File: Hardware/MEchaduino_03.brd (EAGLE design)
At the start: 41.9 x 41.9 mm, 45 parts, among them Q2 NFET, U1 TLV70233PDBVR, U2 ATSAMD51G-M, U3 TXB0104, Y2 32,768Khz

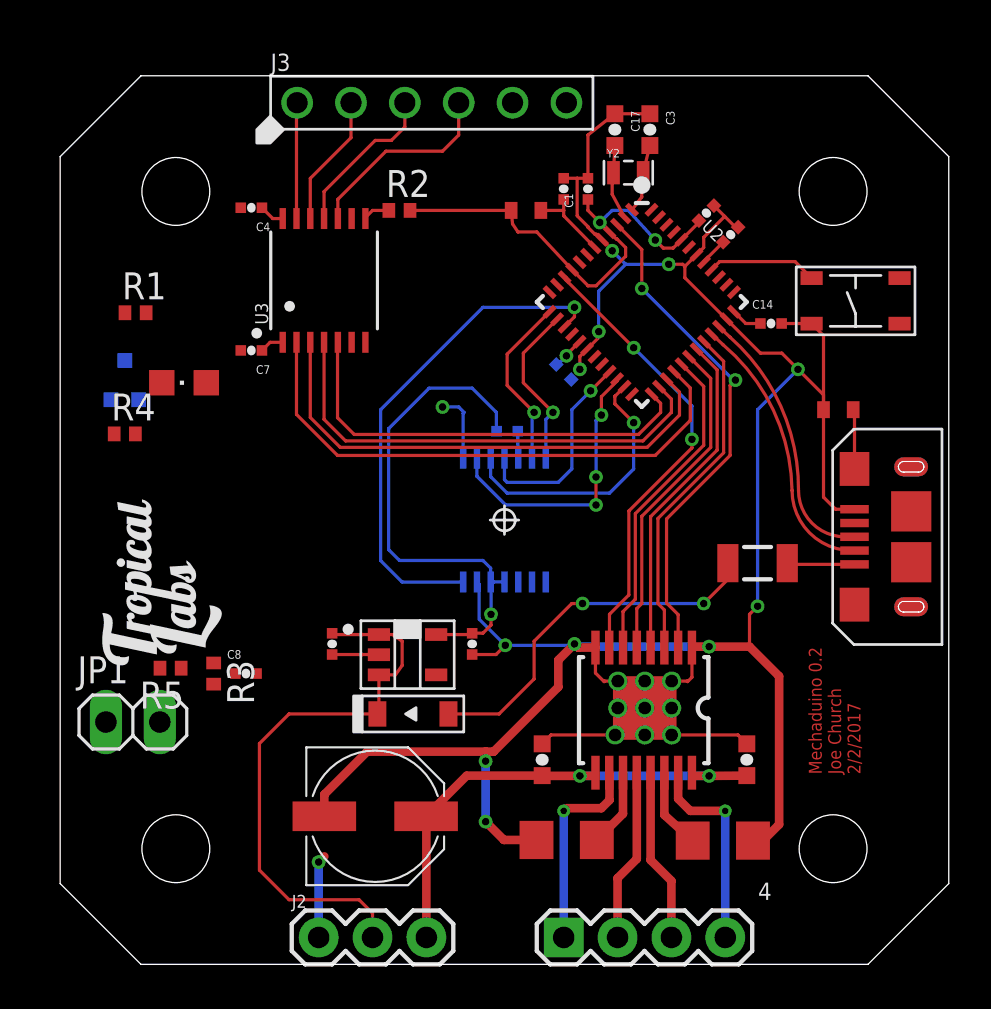
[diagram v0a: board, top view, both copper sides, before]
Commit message: changed microcontroller to ATSAMD51J19
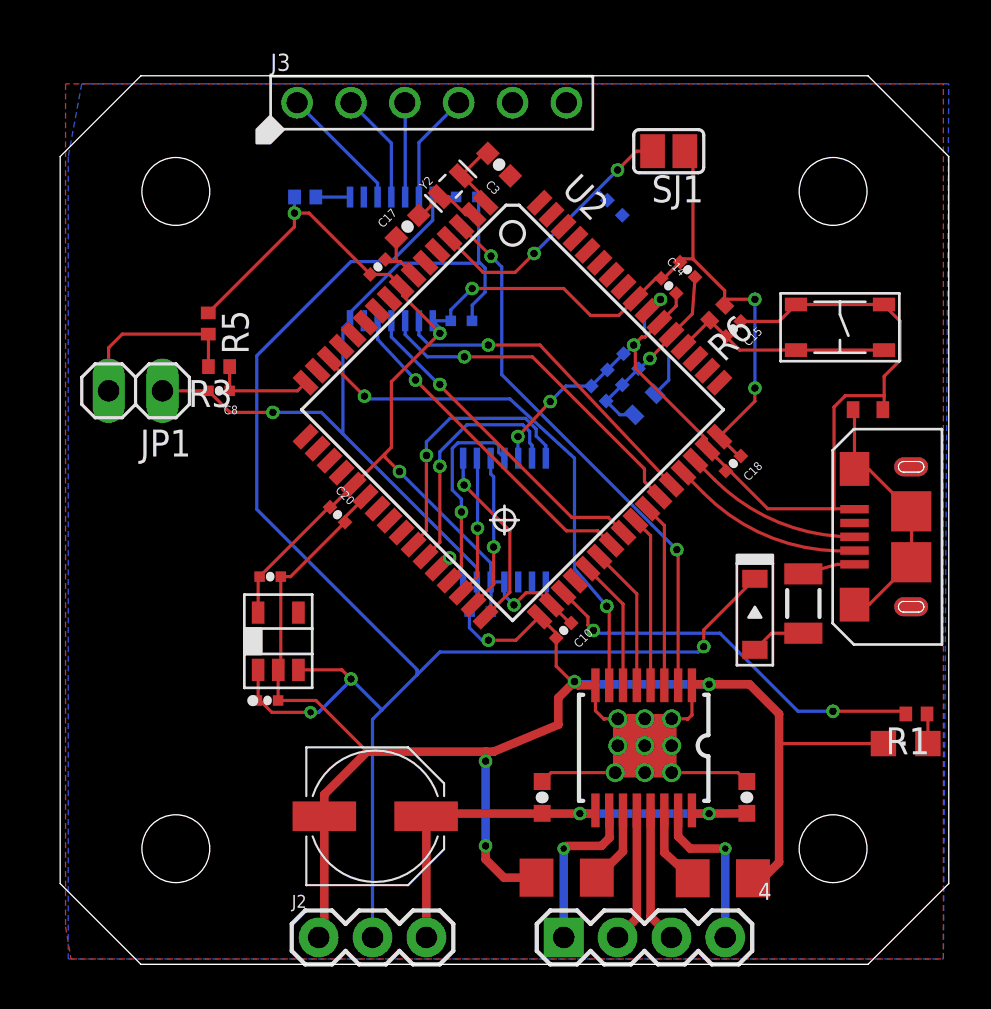
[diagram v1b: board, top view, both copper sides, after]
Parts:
- removed Q2: NFET, SparkFun-DiscreteSemi:SOT323
- removed R4: 100k, rcl:R0402
- removed U$3: TROPICAL_LABS_LOGO_1LOGO3, stepper_servo_prototype_1:LOGO3
- added C15, C18, C20, C21, C22: 0.1uF, swift:0402-CAP
- added R6: 10k, rcl:R0402
- added SJ1: (no value), jumper:SJ
- C17, C3: value 18pF -> 22pF
- R1: value 330 -> 1k
- U2: value ATSAMD51G-M -> ATSAMD51J19; device atsamd51:QFN-48 -> atsamd51:TQFP64
- moved R1 41.4 mm to (40.4, 11.8), turned to 180 degrees
- moved LED1 38.1 mm to (39.9, 10.4)
- moved D1 16.8 mm to (32.8, 16.5), turned to 270 degrees
- moved R5 16.4 mm to (6.99, 30.2), turned to 270 degrees
- moved C2 15.7 mm to (15.0, 32.9)
- moved JP1 15.6 mm to (3.56, 27.1), turned to 180 degrees
- moved R3 14.5 mm to (7.49, 28.2), turned to 180 degrees
- moved C8 13.4 mm to (7.49, 27.1), turned to 180 degrees
- moved C10 12.2 mm to (23.7, 15.7), flipped to the top
- moved C17 10.8 mm to (16.4, 34.8), turned to 45 degrees
- moved L2 10.7 mm to (27.6, 26.4), flipped to the bottom, turned to 135 degrees
- moved C4 10.2 mm to (19.2, 36.2), flipped to the bottom
- moved C19 10.0 mm to (9.91, 18.3), turned to 0 degrees
- moved C7 10.0 mm to (18.9, 30.4), flipped to the bottom
- moved C1 8.98 mm to (26.2, 27.7), flipped to the bottom, turned to 45 degrees
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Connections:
- net PA00_XIN1 renamed CRYST1
- net PA01_XOUT1 renamed CRYST2
- removed net ARDUINO_D13_SCK: Q2.1, R4.2
- removed net GND2: J2.1
- removed net HEADER_MISO: U$4.3, U2.23
- removed net HEADER_MOSI: U$4.4, U2.21
- removed net HEADER_SCK: U$4.2, U2.22
- removed net HEADER_SS: U$4.1, U2.11
- removed net N$11: J3.P$4, U3.10
- removed net N$12: J3.P$3, U3.11
- removed net N$17: J3.P$2, U3.12
- removed net N$18: J3.P$1, U3.13
- removed net N$3: Q2.3, R1.1
- removed net SCL: U2.48
- removed net SDA: U2.47
- removed net TARGET_USB_N: J1.2, U2.33
- removed net TARGET_USB_P: J1.3, U2.34
- removed net VDDANA: C5.1, L2.2, U2.6
- new net AREF: C22.1, SJ1.2, U2.4
- new net D+: J1.3, U2.46
- new net D-: J1.2, U2.45
- new net D13: R1.2, U2.35
- new net MISO: U$4.3, U2.31
- new net MOSI: U$4.4, U2.29
- new net N$10: L2.2, U2.55
- new net N$2: J3.P$4, U3.13
- new net N$4: J3.P$3, U3.12
- new net SCK: U$4.2, U2.30
- new net SS: U$4.1, U2.32
- net 3.3V: now also C10.1, C11.2, C14.1, C18.1, C20.1, R6.1, SJ1.1, U2.21, U2.34, U2.48, U2.56, U2.8; no longer C1.1, L2.1, LED1.A, U2.4, U2.44, U2.9
- net A: now also U2.27; no longer U2.13
- net ARDUINO_D0: now also U2.44, U3.2; no longer U2.25, U3.5
- net ARDUINO_D1: now also U2.43, U3.3; no longer U2.26, U3.4
- net ARDUINO_D2: now also U2.40, U3.4; no longer U2.27, U3.3
- net ARDUINO_D3: now also U2.39, U3.5; no longer U2.28, U3.2
- net B: now also U2.26; no longer U2.14
- net GND: now also C15.1, C18.2, C20.2, C21.2, C22.2, J2.1, LED1.C, SW2.P$4, U2.22, U2.33, U2.47, U2.54, U2.7; no longer C11.2, Q2.2, R4.1, U2.18, U2.35, U2.42, U2.5
- net I: now also U2.28; no longer U2.15
- net IN1: now also U2.37; no longer U2.29
- net IN2: now also U2.38; no longer U2.30
- net IN3: now also U2.42; no longer U2.32
- net IN4: now also U2.41; no longer U2.31
- net N$1: now also LED1.A, R1.1; no longer LED1.C, R1.2
- net N$5: now also J3.P$2, U3.11; no longer C14.1, U2.36
- net N$7: now also J3.P$1, U3.10; no longer C10.1, U2.17
- net N$8: now also C1.1, C21.1, C5.1, L2.1, U2.53; no longer U2.41
- net RESET: now also C15.2, R6.2, SW2.P$2, U2.52; no longer U2.40
- net TH1: now also U2.16; no longer U2.8
- net VREF1: now also U2.14; no longer U2.10
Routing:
- net GND: track 127.9 -> 195.7 mm, vias 19 -> 17
- net VIN: track 28.7 -> 74.6 mm, vias 0 -> 3
- net 3.3V: track 47.7 -> 82.0 mm, vias 3 -> 7
- net I: track 23.7 -> 2.18 mm
- net D13: track 0.00 -> 18.7 mm, vias 0 -> 2
- net N$33: track 17.6 -> 2.61 mm, vias 2 -> 0
- net HEADER_SCK: track 13.4 -> 0.00 mm, vias 3 -> 0
- net AREF: track 0.00 -> 13.3 mm, vias 0 -> 2
- net HEADER_MISO: track 12.9 -> 0.00 mm, vias 1 -> 0
- net TARGET_USB_N: track 12.5 -> 0.00 mm
- net TARGET_USB_P: track 12.2 -> 0.00 mm
- net ARDUINO_D3: track 26.1 -> 16.0 mm, vias 0 -> 1
- net HEADER_MOSI: track 9.83 -> 0.00 mm, vias 1 -> 0
- net MOSI: track 0.00 -> 9.70 mm, vias 0 -> 1
- net N$11: track 9.39 -> 0.00 mm
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- added copper zone on layer 1, net GND
- added copper zone on layer 16, net GND
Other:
- board text removed: "Mechaduino 0.2 Joe Church 2/2/2017"

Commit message: implemted voltage sense pin and some leds
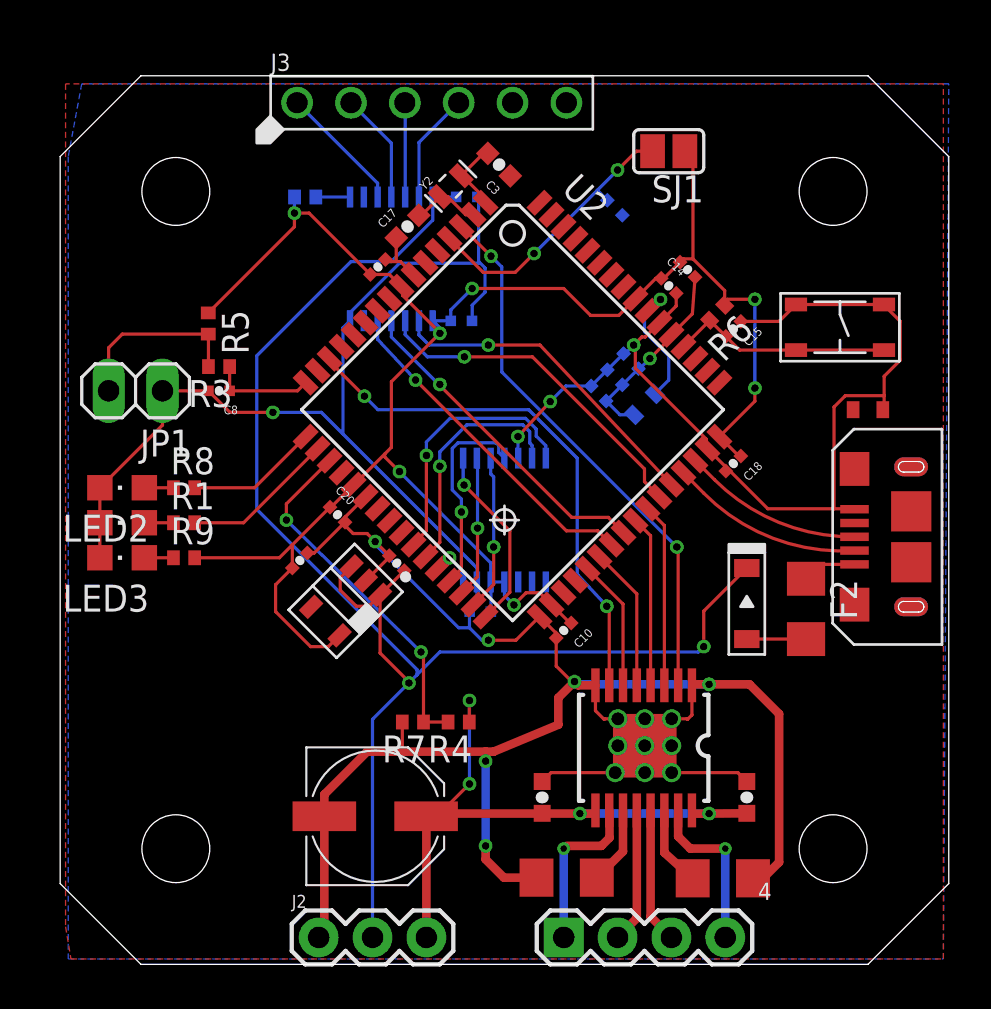
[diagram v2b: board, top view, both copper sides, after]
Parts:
- removed F1: 500mA, SparkFun-PowerIC:PTC-1206
- added F2: 500mA, adafruit:R1206
- added LED2: Red, Opto:CHIPLED_0805
- added LED3: Green, Opto:CHIPLED_0805
- added R4: 100k, rcl:R0402
- added R7: 6k8, rcl:R0402
- added R8, R9: 1k, rcl:R0402
- J1: value (none) -> USB
- J2: value (none) -> power
- J3: value (none) -> signals
- JP1: value (none) -> thermistor
- JP6: value (none) -> Motor
- SJ1: value (none) -> vref
- SW2: value (none) -> Reset
- moved LED1 38.4 mm to (2.92, 20.8)
- moved R1 35.7 mm to (5.84, 20.8), turned to 0 degrees
- moved C9 8.89 mm to (15.9, 18.9), turned to 135 degrees
- moved U1 3.70 mm to (13.5, 17.1), turned to 225 degrees
- moved C19 1.59 mm to (11.3, 19.1), turned to 45 degrees
- moved D1 0.63 mm to (32.4, 17.0)
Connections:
- net SHIELD renamed N$9
- net VIN renamed +5V
- removed net D13: R1.2, U2.35
- removed net N$33: D1.ANODE, F1.2
- new net LEDERROR: R8.2, U2.17
- new net LEDSTATUS: R1.2, U2.18
- new net N$11: LED3.A, R9.1
- new net N$12: D1.ANODE, F2.2
- new net N$3: LED2.A, R8.1
- new net VSENSE: R4.2, R7.1, U2.19
- net 3.3V: now also R9.2
- net GND: now also LED2.C, LED3.C, R7.2
- net N$36: now also F2.1; no longer F1.1
- net V+: now also R4.1
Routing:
- net D13: track 18.7 -> 0.00 mm, vias 2 -> 0
- net VSENSE: track 0.00 -> 17.0 mm, vias 0 -> 2
- net N$9: track 12.3 -> 0.00 mm
- net 3.3V: track 82.0 -> 90.4 mm
- net V+: track 22.7 -> 30.3 mm, vias 2 -> 4
- net LEDSTATUS: track 0.00 -> 7.25 mm
- net LEDERROR: track 0.00 -> 6.23 mm
- net GND: track 195.7 -> 199.2 mm, vias 17 -> 18
- net N$12: track 0.00 -> 2.79 mm
- net N$33: track 2.61 -> 0.00 mm
- net N$3: track 0.00 -> 1.37 mm
- net N$11: track 0.00 -> 1.37 mm
- net +5V: track 74.6 -> 73.5 mm, vias 3 -> 2

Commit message: Rearange to fit old pin positions
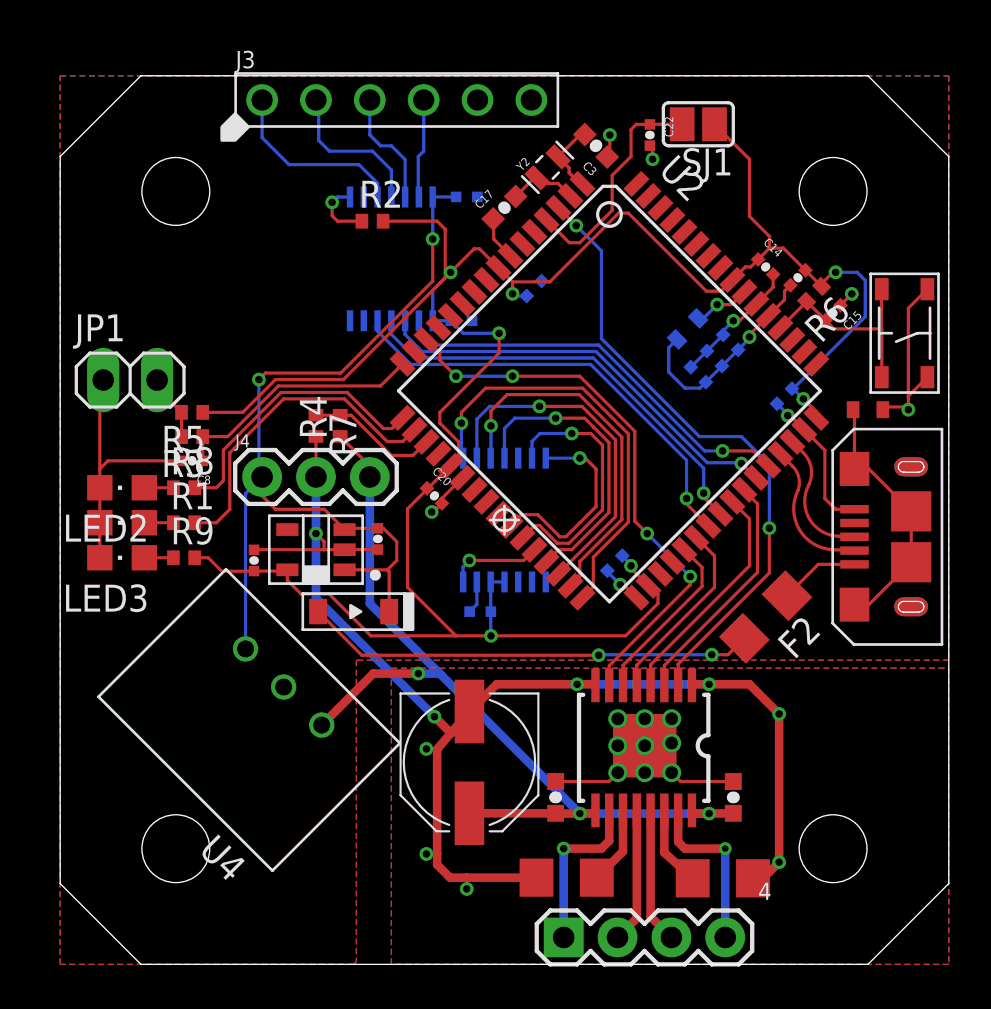
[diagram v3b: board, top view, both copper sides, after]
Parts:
- removed J2: power, SparkFun-Connectors:1X03
- added J4: power, SparkFun-Connectors:1X03
- added U4: R-78E5.0-1.0, SparkFun-IC-Power:DC-DC_CONVERTER_78XX
- moved D1 18.5 mm to (13.8, 16.6), turned to 180 degrees
- moved R4 15.0 mm to (13.2, 25.4), turned to 90 degrees
- moved R7 14.7 mm to (12.1, 25.4), turned to 270 degrees
- moved C2 7.44 mm to (22.4, 31.9), flipped to the bottom, turned to 135 degrees
- moved C11 5.22 mm to (34.8, 32.4), turned to 45 degrees
- moved C12 5.12 mm to (19.3, 9.53), turned to 270 degrees
- moved C1 4.78 mm to (30.9, 28.6)
- moved C21 4.78 mm to (30.1, 27.8)
- moved C5 4.78 mm to (31.6, 29.3)
- moved C15 4.76 mm to (36.4, 30.7)
- moved R6 4.66 mm to (35.6, 31.6)
- moved U2 4.66 mm to (25.9, 27.1)
- moved C14 4.66 mm to (33.3, 32.9)
- moved C20 4.66 mm to (17.7, 22.1)
- moved C17 4.66 mm to (21.0, 35.7)
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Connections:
- net +5V: now also J4.1, U4.VOUT; no longer J2.2
- net GND: now also J4.2, U4.GND; no longer J2.1
- net V+: now also J4.3, U4.VIN; no longer J2.3
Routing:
- net GND: track 199.2 -> 130.6 mm, vias 18 -> 25
- net +5V: track 73.5 -> 42.0 mm
- net 3.3V: track 90.4 -> 116.5 mm
- net N$12: track 2.79 -> 21.3 mm, vias 0 -> 2
- net V+: track 30.3 -> 43.3 mm, vias 4 -> 3
- net N$9: track 0.00 -> 12.2 mm
- net SS: track 8.86 -> 20.1 mm
- net VSENSE: track 17.0 -> 6.27 mm, vias 2 -> 0
- net MISO: track 7.36 -> 17.6 mm
- net SCK: track 6.66 -> 16.7 mm
- net LEDSTATUS: track 7.25 -> 15.4 mm
- net LEDERROR: track 6.23 -> 13.4 mm
- net TH1: track 4.89 -> 12.0 mm
- net N$23: track 8.53 -> 3.14 mm
- net ARDUINO_D3: track 16.0 -> 21.1 mm
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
